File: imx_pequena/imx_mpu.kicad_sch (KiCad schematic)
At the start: 0 parts

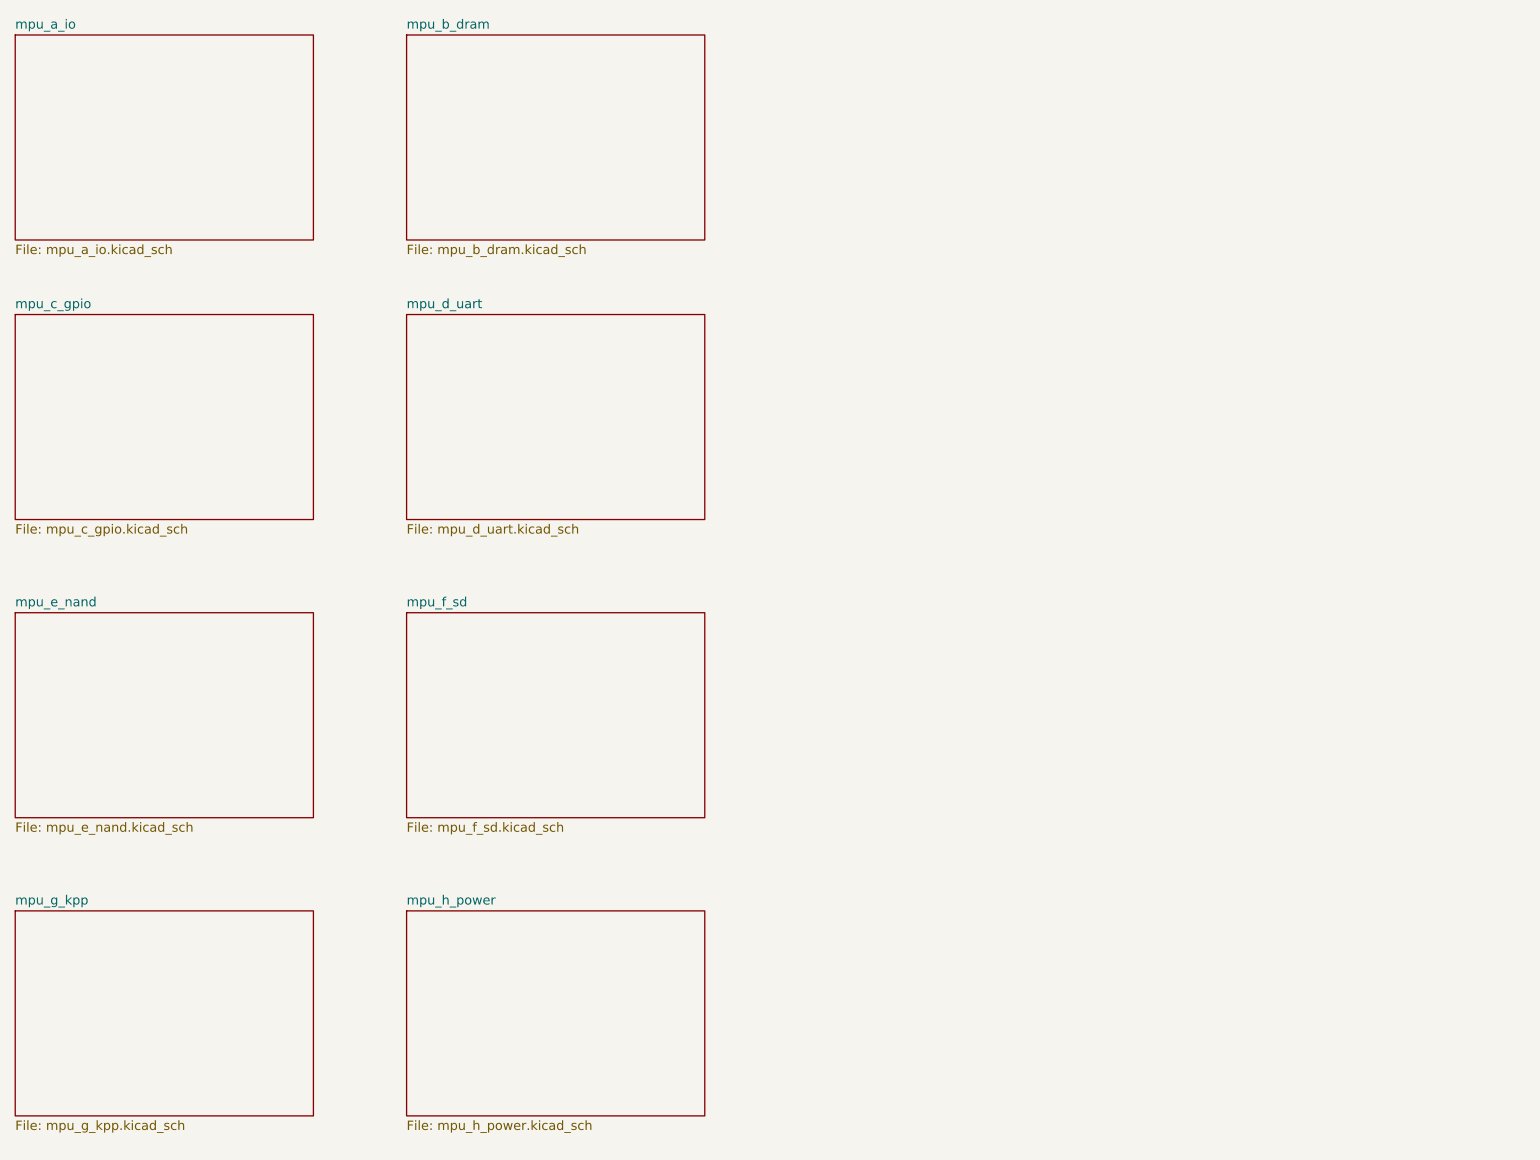
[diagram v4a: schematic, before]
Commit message: USB Updates
Back in the saddle after moving. Added USB C and USB OTG symbols and supporting passives.
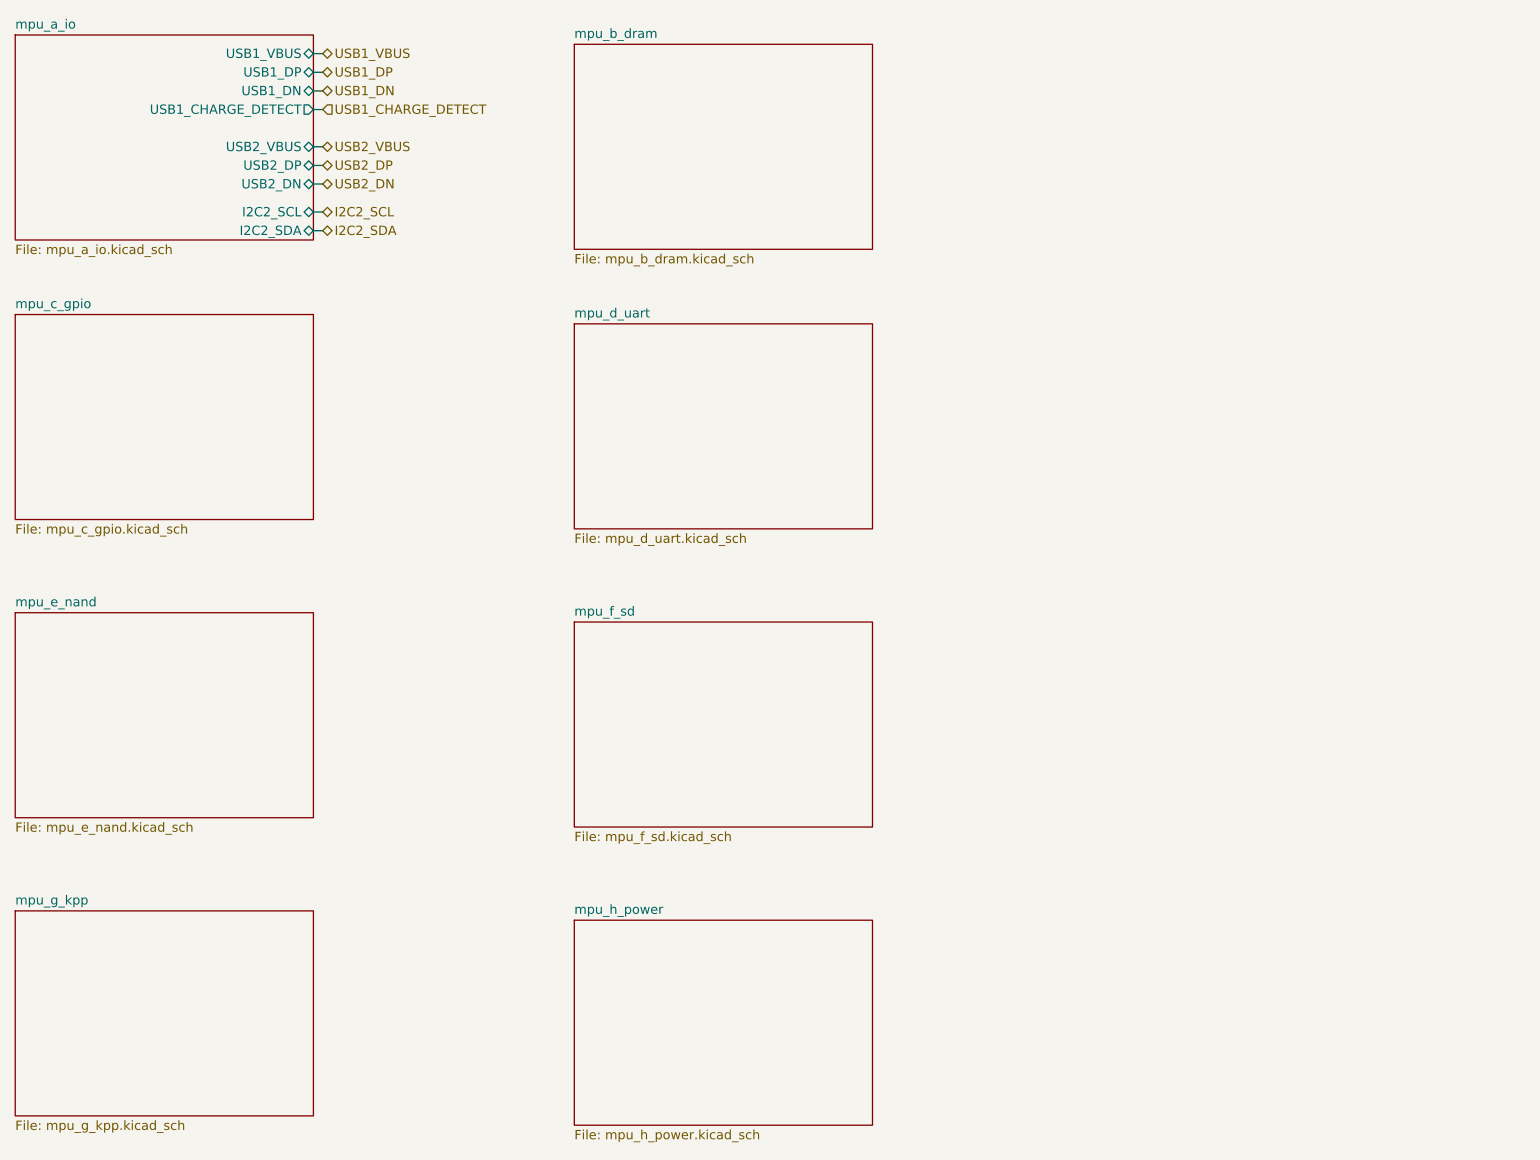
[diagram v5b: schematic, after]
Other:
- sheet mpu_a_io ports: added I2C2_SCL, I2C2_SDA, USB1_CHARGE_DETECT, USB1_DN, USB1_DP, USB1_VBUS, USB2_DN, USB2_DP, USB2_VBUS; removed none
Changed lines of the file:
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@@
 (kicad_sch (version 20211123) (generator eeschema)
   (paper "A4")
-  (sheet (at 83.82 149.86) (size 40.64 27.94) (fields_autoplaced)
+  (wire (pts (xy 71.12 54.61) (xy 72.39 54.61))
+    (stroke (width 0) (type default) (color 0 0 0 0))
+  )
+  (wire (pts (xy 71.12 57.15) (xy 72.39 57.15))
+    (stroke (width 0) (type default) (color 0 0 0 0))
+  )
+  (wire (pts (xy 71.12 48.26) (xy 72.39 48.26))
+    (stroke (width 0) (type default) (color 0 0 0 0))
+  )
+  (wire (pts (xy 71.12 40.64) (xy 72.39 40.64))
+    (stroke (width 0) (type default) (color 0 0 0 0))
+  )
+  (wire (pts (xy 71.12 45.72) (xy 72.39 45.72))
+    (stroke (width 0) (type default) (color 0 0 0 0))
+  )
+  (wire (pts (xy 71.12 35.56) (xy 72.39 35.56))
+    (stroke (width 0) (type default) (color 0 0 0 0))
+  )
+  (wire (pts (xy 71.12 33.02) (xy 72.39 33.02))
+    (stroke (width 0) (type default) (color 0 0 0 0))
+  )
+  (wire (pts (xy 71.12 38.1) (xy 72.39 38.1))
+    (stroke (width 0) (type default) (color 0 0 0 0))
+  )
+  (wire (pts (xy 71.12 50.8) (xy 72.39 50.8))
+    (stroke (width 0) (type default) (color 0 0 0 0))
+  )
+  (hierarchical_label "USB1_DN" (shape bidirectional) (at 72.39 38.1 0)
+    (effects (font (size 1.27 1.27)) (justify left))
+  )
+  (hierarchical_label "I2C2_SCL" (shape bidirectional) (at 72.39 54.61 0)
+    (effects (font (size 1.27 1.27)) (justify left))
+  )
+  (hierarchical_label "USB1_VBUS" (shape bidirectional) (at 72.39 33.02 0)
+    (effects (font (size 1.27 1.27)) (justify left))
+  )
+  (hierarchical_label "USB2_DP" (shape bidirectional) (at 72.39 48.26 0)
+    (effects (font (size 1.27 1.27)) (justify left))
+  )
+  (hierarchical_label "USB1_CHARGE_DETECT" (shape input) (at 72.39 40.64 0)
+    (effects (font (size 1.27 1.27)) (justify left))
+  )
+  (hierarchical_label "USB1_DP" (shape bidirectional) (at 72.39 35.56 0)
+    (effects (font (size 1.27 1.27)) (justify left))
+  )
+  (hierarchical_label "USB2_VBUS" (shape bidirectional) (at 72.39 45.72 0)
+    (effects (font (size 1.27 1.27)) (justify left))
+  )
+  (hierarchical_label "USB2_DN" (shape bidirectional) (at 72.39 50.8 0)
+    (effects (font (size 1.27 1.27)) (justify left))
+  )
+  (hierarchical_label "I2C2_SDA" (shape bidirectional) (at 72.39 57.15 0)
+    (effects (font (size 1.27 1.27)) (justify left))
+  )
+  (sheet (at 106.68 151.13) (size 40.64 27.94) (fields_autoplaced)
     (stroke (width 0.1524) (type solid) (color 0 0 0 0))
     (fill (color 0 0 0 0.0000))
-    (property "Sheet name" "mpu_h_power" (id 0) (at 83.82 149.1484 0)
+    (property "Sheet name" "mpu_h_power" (id 0) (at 106.68 150.4184 0)
       (effects (font (size 1.27 1.27)) (justify left bottom))
     )
-    (property "Sheet file" "mpu_h_power.kicad_sch" (id 1) (at 83.82 178.3846 0)
+    (property "Sheet file" "mpu_h_power.kicad_sch" (id 1) (at 106.68 179.6546 0)
       (effects (font (size 1.27 1.27)) (justify left top))
     )
@@
     )
   )
-  (sheet (at 83.82 68.58) (size 40.64 27.94) (fields_autoplaced)
+  (sheet (at 106.68 69.85) (size 40.64 27.94) (fields_autoplaced)
     (stroke (width 0.1524) (type solid) (color 0 0 0 0))
     (fill (color 0 0 0 0.0000))
-    (property "Sheet name" "mpu_d_uart" (id 0) (at 83.82 67.8684 0)
+    (property "Sheet name" "mpu_d_uart" (id 0) (at 106.68 69.1384 0)
       (effects (font (size 1.27 1.27)) (justify left bottom))
     )
-    (property "Sheet file" "mpu_d_uart.kicad_sch" (id 1) (at 83.82 97.1046 0)
+    (property "Sheet file" "mpu_d_uart.kicad_sch" (id 1) (at 106.68 98.3746 0)
       (effects (font (size 1.27 1.27)) (justify left top))
     )
@@
       (effects (font (size 1.27 1.27)) (justify left top))
     )
+    (pin "I2C2_SDA" bidirectional (at 71.12 57.15 0)
+      (effects (font (size 1.27 1.27)) (justify right))
+    )
+    (pin "I2C2_SCL" bidirectional (at 71.12 54.61 0)
+      (effects (font (size 1.27 1.27)) (justify right))
+    )
+    (pin "USB1_VBUS" bidirectional (at 71.12 33.02 0)
+      (effects (font (size 1.27 1.27)) (justify right))
+    )
+    (pin "USB2_DP" bidirectional (at 71.12 48.26 0)
+      (effects (font (size 1.27 1.27)) (justify right))
+    )
+    (pin "USB2_DN" bidirectional (at 71.12 50.8 0)
+      (effects (font (size 1.27 1.27)) (justify right))
+    )
+    (pin "USB1_DP" bidirectional (at 71.12 35.56 0)
+      (effects (font (size 1.27 1.27)) (justify right))
+    )
+    (pin "USB1_CHARGE_DETECT" output (at 71.12 40.64 0)
+      (effects (font (size 1.27 1.27)) (justify right))
+    )
+    (pin "USB1_DN" bidirectional (at 71.12 38.1 0)
+      (effects (font (size 1.27 1.27)) (justify right))
+    )
+    (pin "USB2_VBUS" bidirectional (at 71.12 45.72 0)
+      (effects (font (size 1.27 1.27)) (justify right))
+    )
   )
-  (sheet (at 83.82 109.22) (size 40.64 27.94) (fields_autoplaced)
+  (sheet (at 106.68 110.49) (size 40.64 27.94) (fields_autoplaced)
     (stroke (width 0.1524) (type solid) (color 0 0 0 0))
     (fill (color 0 0 0 0.0000))
-    (property "Sheet name" "mpu_f_sd" (id 0) (at 83.82 108.5084 0)
+    (property "Sheet name" "mpu_f_sd" (id 0) (at 106.68 109.7784 0)
       (effects (font (size 1.27 1.27)) (justify left bottom))
     )
-    (property "Sheet file" "mpu_f_sd.kicad_sch" (id 1) (at 83.82 137.7446 0)
+    (property "Sheet file" "mpu_f_sd.kicad_sch" (id 1) (at 106.68 139.0146 0)
       (effects (font (size 1.27 1.27)) (justify left top))
     )
   )
-  (sheet (at 83.82 30.48) (size 40.64 27.94) (fields_autoplaced)
+  (sheet (at 106.68 31.75) (size 40.64 27.94) (fields_autoplaced)
     (stroke (width 0.1524) (type solid) (color 0 0 0 0))
     (fill (color 0 0 0 0.0000))
-    (property "Sheet name" "mpu_b_dram" (id 0) (at 83.82 29.7684 0)
+    (property "Sheet name" "mpu_b_dram" (id 0) (at 106.68 31.0384 0)
       (effects (font (size 1.27 1.27)) (justify left bottom))
     )
-    (property "Sheet file" "mpu_b_dram.kicad_sch" (id 1) (at 83.82 59.0046 0)
+    (property "Sheet file" "mpu_b_dram.kicad_sch" (id 1) (at 106.68 60.2746 0)
       (effects (font (size 1.27 1.27)) (justify left top))
     )

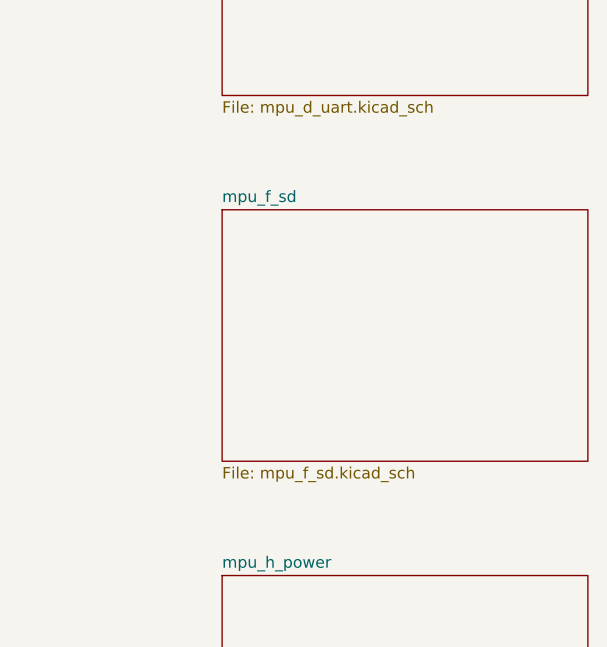
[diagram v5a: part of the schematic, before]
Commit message: Power upates
Added connections to power pins and decoupling caps
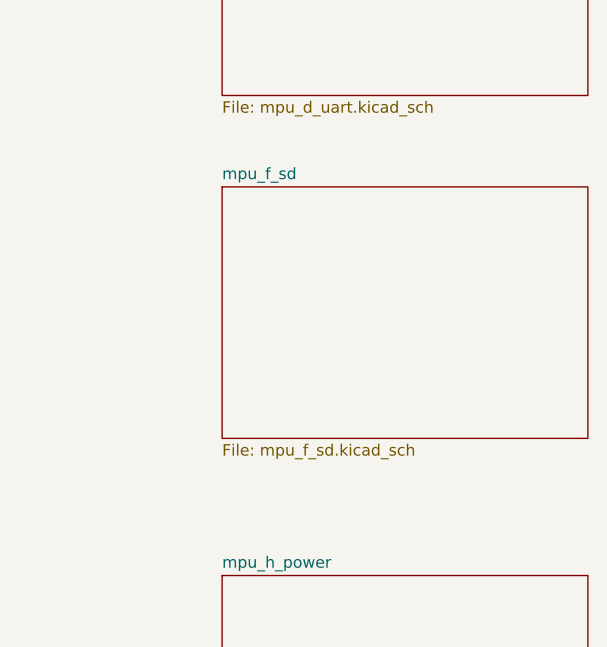
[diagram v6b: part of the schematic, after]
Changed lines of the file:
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@@
     )
   )
-  (sheet (at 106.68 110.49) (size 40.64 27.94) (fields_autoplaced)
+  (sheet (at 106.68 107.95) (size 40.64 27.94) (fields_autoplaced)
     (stroke (width 0.1524) (type solid) (color 0 0 0 0))
     (fill (color 0 0 0 0.0000))
-    (property "Sheet name" "mpu_f_sd" (id 0) (at 106.68 109.7784 0)
+    (property "Sheet name" "mpu_f_sd" (id 0) (at 106.68 107.2384 0)
       (effects (font (size 1.27 1.27)) (justify left bottom))
     )
-    (property "Sheet file" "mpu_f_sd.kicad_sch" (id 1) (at 106.68 139.0146 0)
+    (property "Sheet file" "mpu_f_sd.kicad_sch" (id 1) (at 106.68 136.4746 0)
       (effects (font (size 1.27 1.27)) (justify left top))
     )
